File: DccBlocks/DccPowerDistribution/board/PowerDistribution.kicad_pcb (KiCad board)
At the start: 4 copper layers, 95 x 46 mm, 66 parts, among them J1 Conn_01x02, J2 Conn_01x02, J3 Conn_01x03, J4 Conn_01x02, J5 Conn_01x02, J6 Conn_01x02, J7 Conn_01x04, J8 Conn_01x02, Q1 BC857, Q2 BC817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

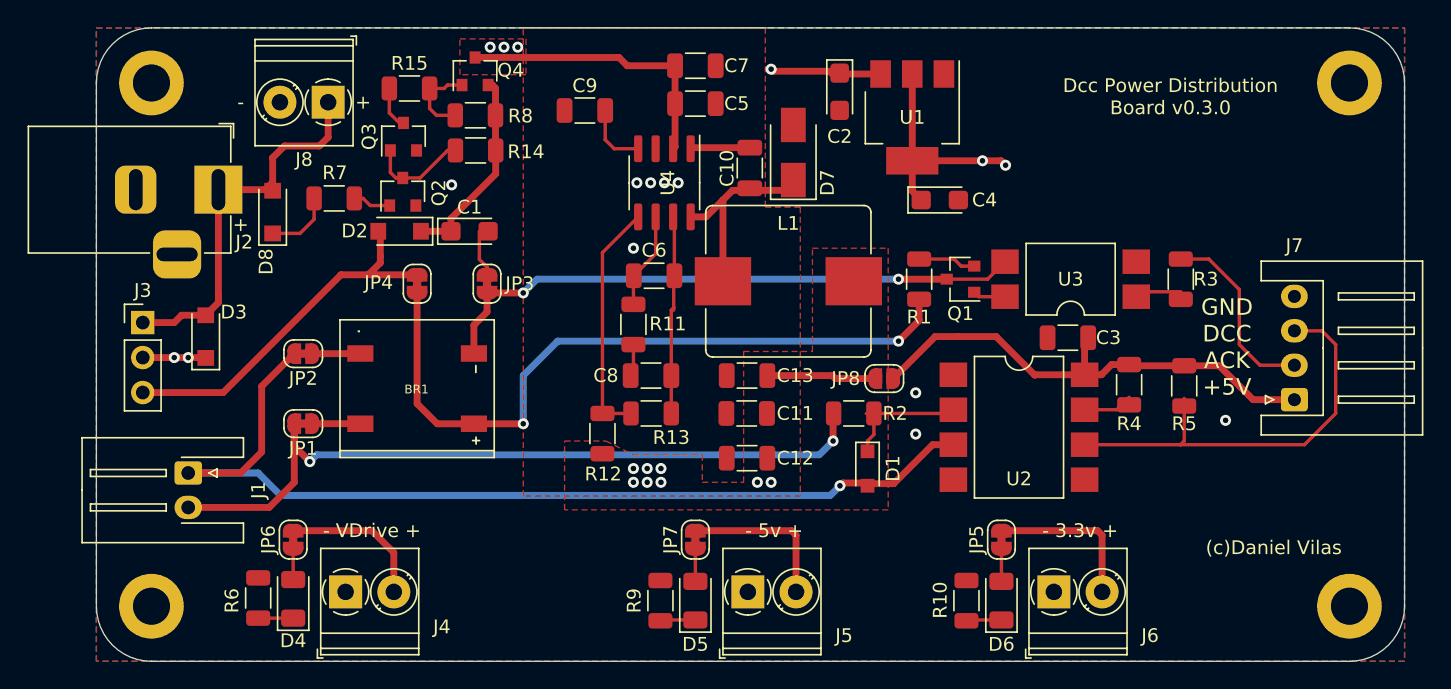
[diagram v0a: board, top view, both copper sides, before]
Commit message: Added filtering caps and kibot under docker
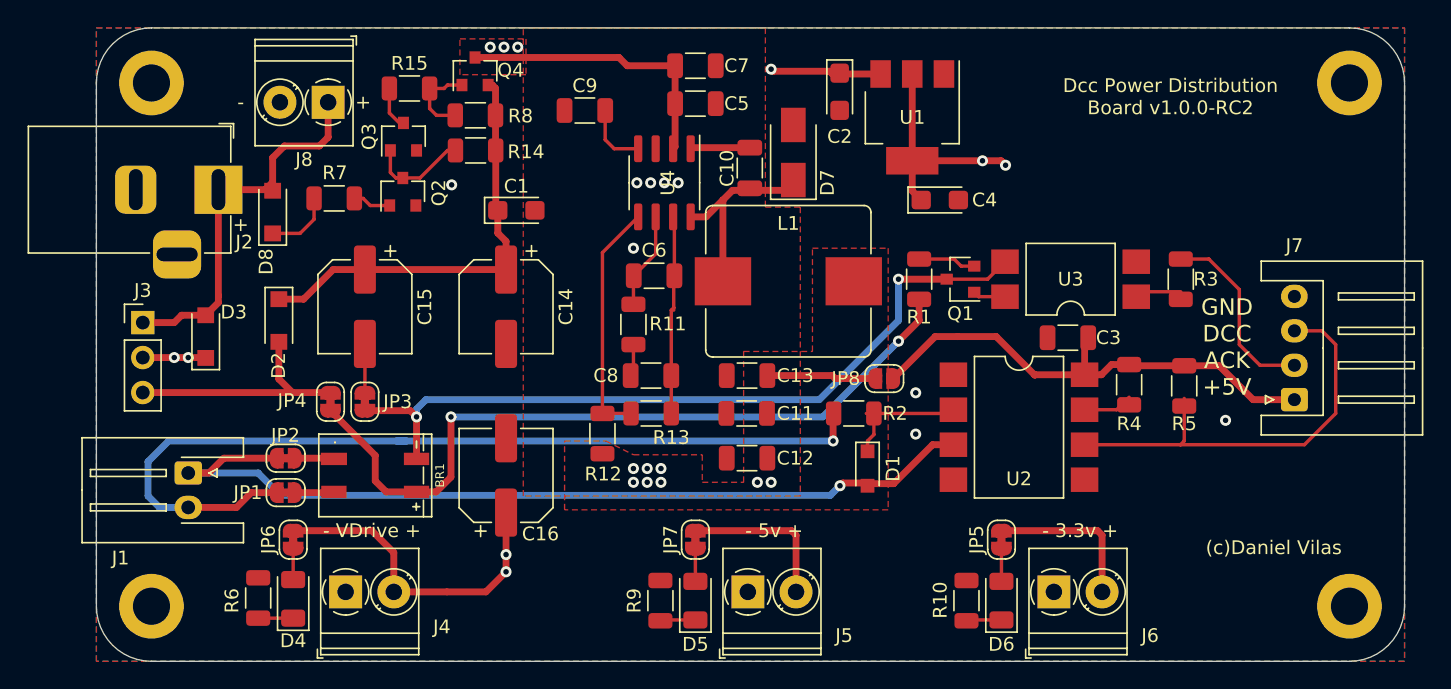
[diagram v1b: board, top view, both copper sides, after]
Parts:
- added C14: 100uf, Capacitor_SMD:CP_Elec_6.3x7.7, F.Cu at (49.8, 40.2)
- added C15: 100uf, Capacitor_SMD:CP_Elec_6.3x7.7, F.Cu at (39.5, 40.2)
- added C16: 100uf, Capacitor_SMD:CP_Elec_6.3x7.7, F.Cu at (49.8, 52.5)
- BR1: value DB107S -> KMB26STR; footprint Project:DIOB_DB107S -> Project:DIOB_KMB26S
- moved JP3 12.3 mm to (39.5, 47.1)
- moved D2 10.9 mm to (33.2, 41.2), turned to 270 degrees
- moved JP4 10.6 mm to (37.0, 47.1)
- moved JP2 7.70 mm to (33.8, 51.2)
- moved BR1 7.00 mm to (40.2, 52.5)
- moved JP1 5.17 mm to (33.8, 53.8)
- moved C1 3.72 mm to (50.5, 33.2)
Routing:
- net /Power Distribution/_DccVinP: track 14.5 -> 31.9 mm
- net /Dcc Interface/DccP-: track 43.4 -> 56.5 mm
- net Vdrive: track 36.3 -> 49.3 mm, vias 5 -> 7
- net /Dcc Interface/DccPower: track 26.9 -> 17.7 mm
- net /Dcc Interface/J: track 56.6 -> 65.5 mm, vias 2 -> 1
- net /Dcc Interface/K: track 71.9 -> 64.7 mm
- net /Dcc Interface/DccP+: track 51.8 -> 55.5 mm
- net /Dcc Interface/K_ACK: track 3.50 -> 2.87 mm
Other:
- board text added: "Dcc Power Distribution Board v1.0.0-RC2"
- board text removed: "Dcc Power Distribution Board v0.3.0"

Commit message: Update kibot, clean drc,...
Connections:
- net /5V_iFace renamed /5V_iface
- net /Dcc Interface/DccPower renamed /Power Distribution/_DccVin
- net /Power Distribution/Vin renamed /Power Distribution/_Vin
- U2 pad 1: (no net) -> unconnected-(U2-Pad1)
- U4 pad 3: (no net) -> unconnected-(U4-Pad3)
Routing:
- net /Dcc Interface/J: track 65.5 -> 64.8 mm
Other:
- net class Default removed
- net class Power removed

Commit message: Updates
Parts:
- added JP9: SolderJumper_2_Open, Jumper:SolderJumper-2_P1.3mm_Open_RoundedPad1.0x1.5mm, F.Cu at (102.9, 53.2)
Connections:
- net +3V3 renamed +3.3V
- net /Power Distribution/_DccVin renamed /Power Distribution/DccVin
- net /Power Distribution/_Vin renamed /Power Distribution/Vin
- C3 pad 2: GND -> /GND_iface
- J7 pad 4: GND -> /GND_iface
- U2 pad 5: GND -> /GND_iface
- U3 pad 2: GND -> /GND_iface
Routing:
- net /GND_iface: track 0.00 -> 74.7 mm
- net GND: vias 9 -> 11

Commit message: Update Kibot Scripts to latest versions
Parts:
- moved R1 0.12 mm to (79.6, 38.2)
